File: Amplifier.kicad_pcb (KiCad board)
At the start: 2 copper layers, 63 x 100 mm, 26 parts, among them J1 Input, J2 Conn_01x04, J3 output, T1 Transformer_SP_1S, U1 6N2P, U2 6P14P

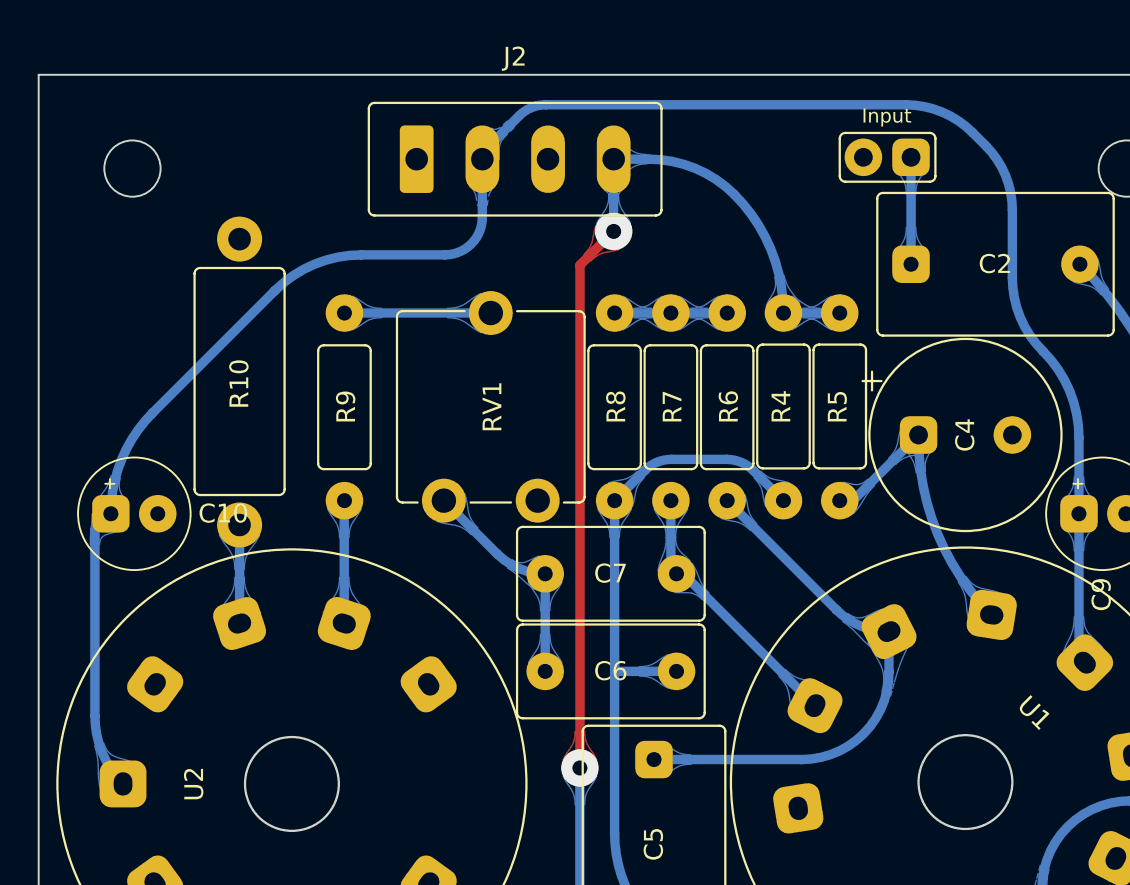
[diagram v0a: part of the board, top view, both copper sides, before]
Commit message: Neon bulb added on the amplifier PCB
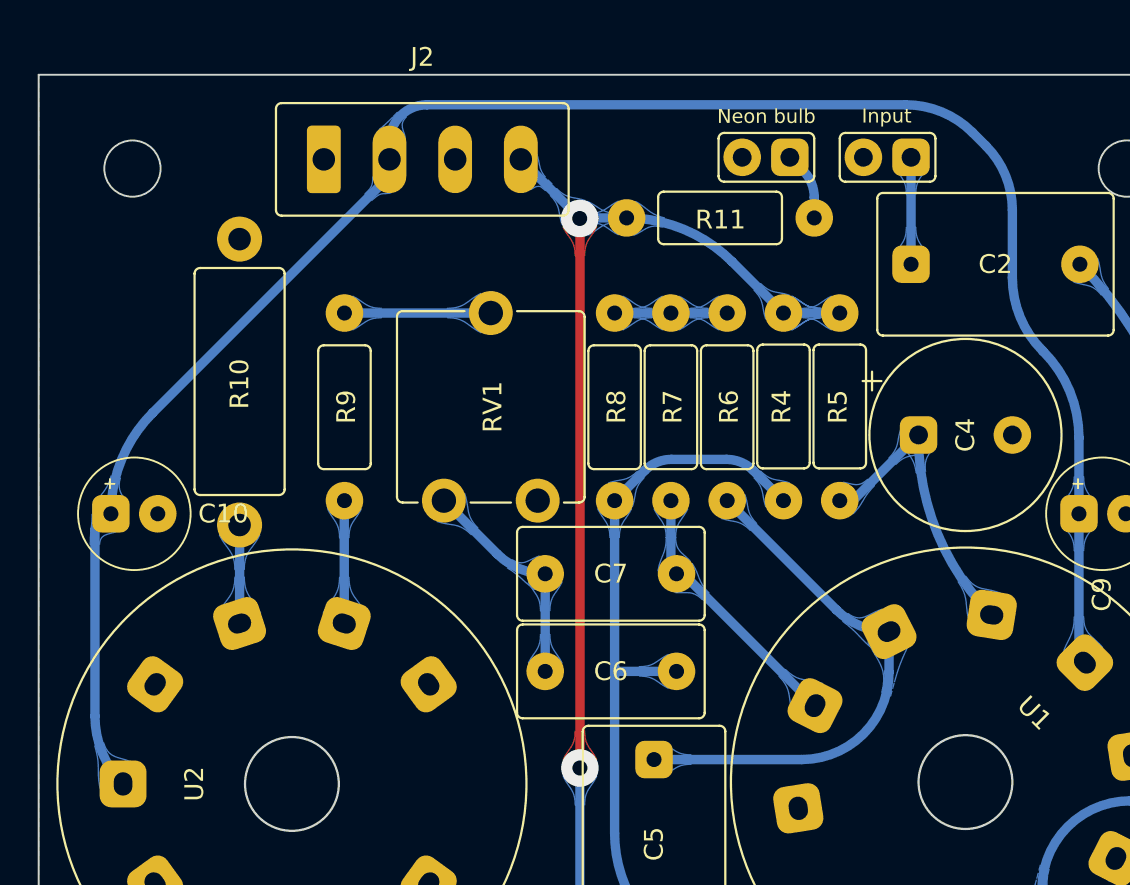
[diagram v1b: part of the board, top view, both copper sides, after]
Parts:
- added J4: Neon bulb, spdf1626_lib:PinHeader_1x02_P2.54mm, F.Cu at (97.0, 44.4)
- added R11: 1M, spdf1626_lib:R_THT_025W, F.Cu at (93.3, 47.6)
- moved J2 4.95 mm to (77.5, 44.5)
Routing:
- net Net-(J4-Pad1): track 0.00 -> 3.67 mm
- net 240V: track 85.8 -> 85.1 mm
- net +6V: track 103.7 -> 103.2 mm

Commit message: Temp
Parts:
- removed T1: Transformer_SP_1S, spdf1626_lib:Output_transformer
- added C1: 10uF, spdf1626_lib:C_THT_D10.0mm_P5.00mm, F.Cu at (64.7, 56.3)
- J2: value Conn_01x04 -> Power
- J3: value output -> Transformer; footprint spdf1626_lib:PinHeader_1x02_P2.54mm -> spdf1626_lib:MCV_1,5_4-G-3.5_1x03_P3.50mm_Vertical
- moved J4 51.6 mm to (101.2, 95.8)
- moved J3 48.9 mm to (76.5, 93.8), turned to 180 degrees
- moved R11 44.9 mm to (100.0, 92.0)
- moved R9 1.10 mm to (74.4, 57.7)
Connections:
- J3 pad 1: Left_output -> 240V
- J3 pad 2: GND -> Net-(U2-Pad9)
- U2 pad 7: Net-(T1-Pad3) -> Net-(U2-Pad7)
- U2 pad 9: Net-(T1-Pad2) -> Net-(U2-Pad9)
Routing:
- net Net-(T1-Pad2): track 30.7 -> 0.00 mm
- net Net-(T1-Pad3): track 19.9 -> 0.00 mm
- net Net-(U2-Pad7): track 0.00 -> 11.2 mm
- net Net-(U2-Pad9): track 0.00 -> 11.2 mm
- net Left_output: track 8.39 -> 0.00 mm
- net 240V: track 85.1 -> 80.4 mm
- net Net-(J4-Pad1): track 3.67 -> 5.35 mm
- net Net-(R9-Pad1): track 7.80 -> 6.70 mm
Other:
- board size 63 x 100 mm -> 68 x 64 mm

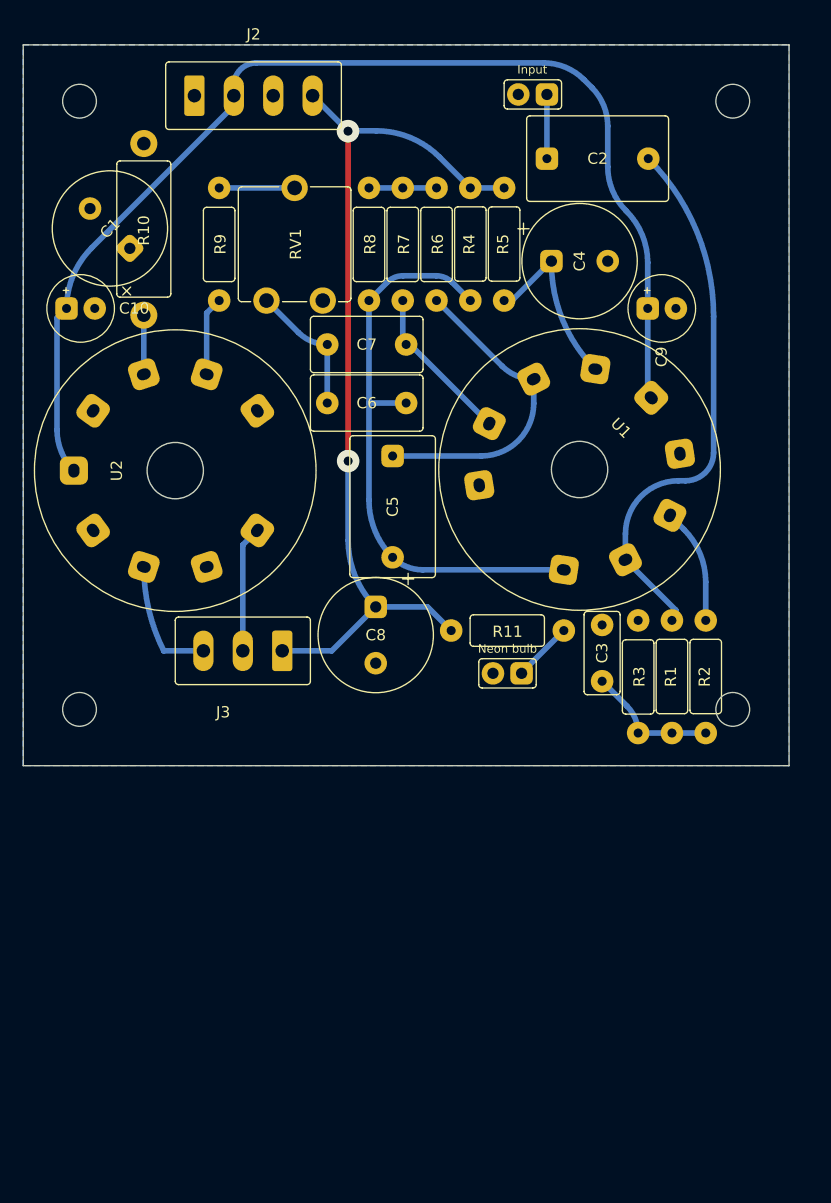
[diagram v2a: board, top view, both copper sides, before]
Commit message: New amplifier PCB with external transformer
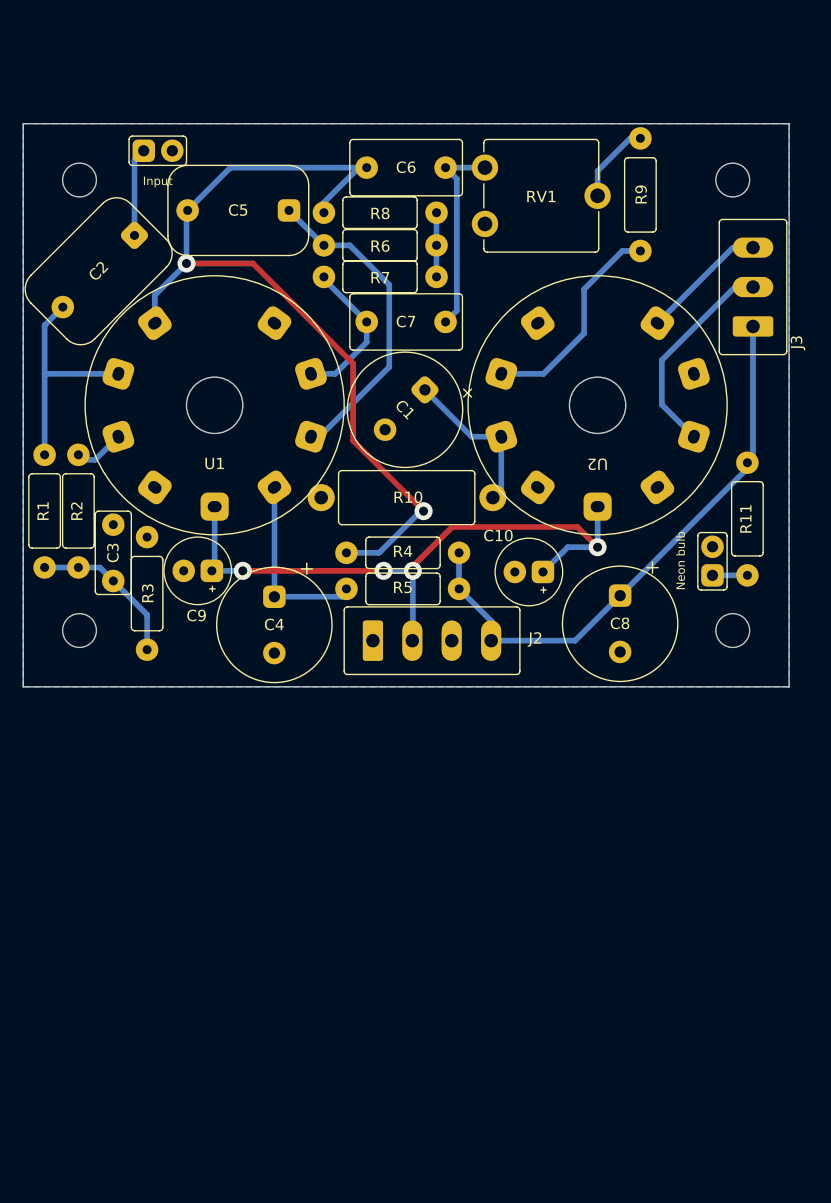
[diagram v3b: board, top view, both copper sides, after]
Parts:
- moved R1 57.6 mm to (58.9, 81.4)
- moved R2 57.6 mm to (61.9, 81.4)
- moved J3 55.6 mm to (121.8, 61.5), turned to 90 degrees
- moved J2 50.9 mm to (93.3, 92.9)
- moved C9 47.3 mm to (72.5, 86.7), turned to 180 degrees
- moved C10 46.2 mm to (101.9, 86.8), turned to 180 degrees
- moved C2 45.4 mm to (63.7, 60.1), turned to -135 degrees
- moved C3 44.3 mm to (65.0, 87.6)
- moved R3 44.2 mm to (68.0, 88.7)
- moved C4 42.2 mm to (79.3, 91.5), turned to -90 degrees
- moved U2 37.9 mm to (108.0, 72.0), turned to 180 degrees
- moved R9 37.7 mm to (111.8, 53.3)
- moved J1 36.1 mm to (67.7, 49.4), turned to 90 degrees
- moved R10 35.0 mm to (98.7, 80.2), turned to 180 degrees
- moved U1 32.9 mm to (74.0, 72.0), turned to 180 degrees
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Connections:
- J3 pad 2: Net-(U2-Pad9) -> Net-(U2-Pad7)
- J3 pad 3: Net-(U2-Pad7) -> Net-(U2-Pad9)
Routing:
- net +6V: track 103.2 -> 58.2 mm, vias 0 -> 4
- net 240V: track 80.4 -> 50.9 mm, vias 2 -> 0
- net Net-(C2-Pad2): track 48.9 -> 20.3 mm
- net Net-(C5-Pad2): track 52.7 -> 77.2 mm, vias 0 -> 2
- net Net-(R9-Pad2): track 7.01 -> 19.2 mm
- net Net-(R10-Pad1): track 5.25 -> 14.3 mm
- net Net-(U2-Pad7): track 11.2 -> 18.8 mm
- net Net-(C6-Pad2): track 12.0 -> 18.0 mm
- net Net-(R2-Pad2): track 10.3 -> 4.58 mm
- net Net-(J4-Pad1): track 5.35 -> 3.10 mm
- net Net-(C3-Pad1): track 11.8 -> 13.9 mm
- net Net-(C2-Pad1): track 5.70 -> 7.86 mm
- net Net-(C7-Pad1): track 14.3 -> 13.5 mm
- net Net-(R9-Pad1): track 6.70 -> 7.20 mm
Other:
- board size 68 x 64 mm -> 68 x 50 mm

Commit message: New Amplifier PCB almost ready
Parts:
- J2: footprint spdf1626_lib:MCV_1,5_4-G-3.5_1x04_P3.50mm_Vertical -> spdf1626_lib:MCV_1,5_4-G-5.0_1x04_P5.0mm_Vertical
- J3: footprint spdf1626_lib:MCV_1,5_4-G-3.5_1x03_P3.50mm_Vertical -> spdf1626_lib:MCV_1,5_4-G-5.0_1x03_P5.0mm_Vertical
- moved C10 12.5 mm to (114.3, 85.2), turned to 0 degrees
- moved R11 12.0 mm to (121.9, 70.1)
- moved R9 10.5 mm to (103.1, 59.2), turned to 180 degrees
- moved C3 8.02 mm to (58.9, 82.4), turned to 0 degrees
- moved R5 7.66 mm to (84.3, 84.1)
- moved R1 7.20 mm to (58.9, 74.2)
- moved R2 7.20 mm to (61.9, 74.2)
- moved J3 7.08 mm to (119.5, 54.8)
- moved C9 5.97 mm to (69.4, 91.8), turned to -90 degrees
- moved R3 5.14 mm to (63.9, 85.6), turned to 180 degrees
- moved J4 4.52 mm to (121.9, 84.5), turned to 0 degrees
- moved R4 3.74 mm to (94.3, 84.1), turned to 180 degrees
- moved J2 1.43 mm to (93.6, 91.5)
- moved C4 1.20 mm to (78.1, 91.4)
- moved C8 0.98 mm to (109.1, 91.8)
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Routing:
- net 240V: track 50.9 -> 63.6 mm
- net Net-(R9-Pad2): track 19.2 -> 10.6 mm
- net Net-(U2-Pad9): track 11.3 -> 19.3 mm
- net Net-(C4-Pad1): track 16.6 -> 10.1 mm
- net Net-(J4-Pad1): track 3.10 -> 9.40 mm
- net Net-(U2-Pad7): track 18.8 -> 24.9 mm
- net Net-(C2-Pad2): track 20.3 -> 14.6 mm
- net Net-(C3-Pad1): track 13.9 -> 9.40 mm
- net +6V: track 58.2 -> 61.8 mm
- net Net-(R2-Pad2): track 4.58 -> 7.06 mm
- net Net-(C5-Pad2): track 77.2 -> 78.4 mm
- net Net-(C7-Pad1): track 13.5 -> 12.3 mm
- net Net-(R9-Pad1): track 7.20 -> 6.50 mm
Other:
- outline, holes or cut-outs redrawn

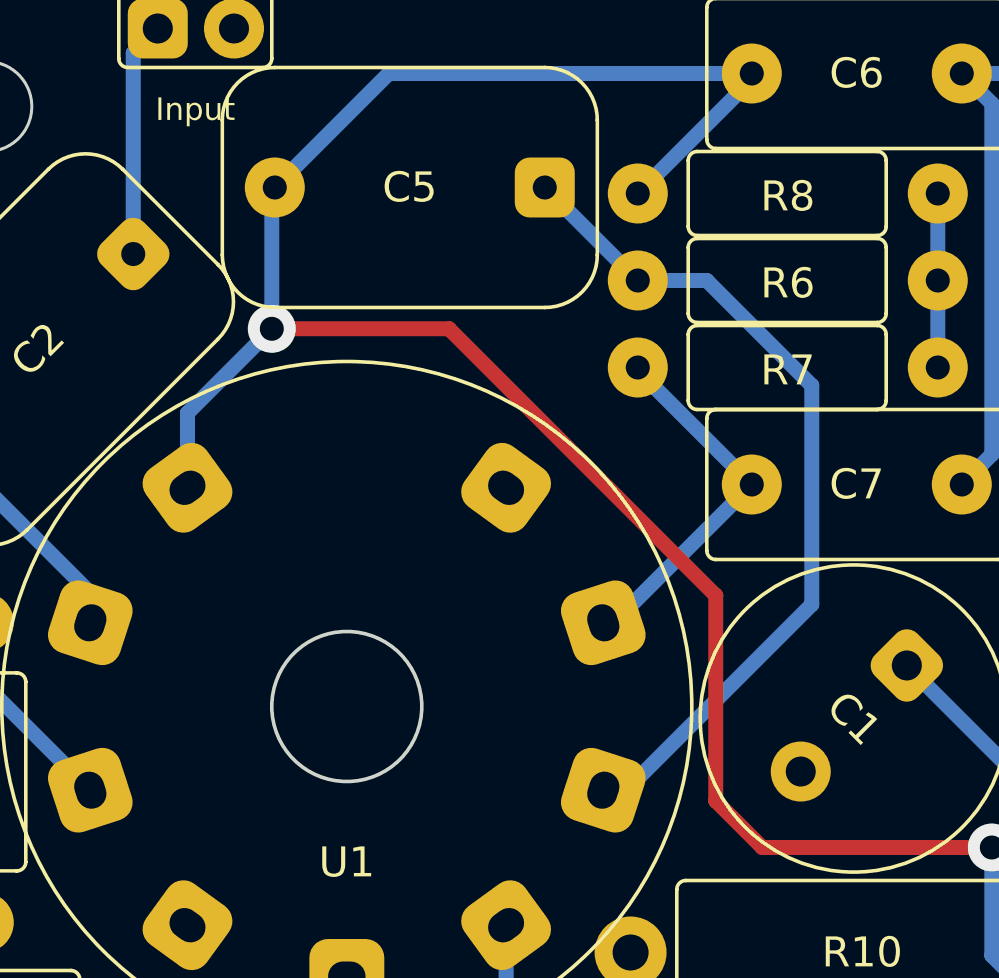
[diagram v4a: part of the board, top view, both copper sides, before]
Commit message: Power supply PCB updated
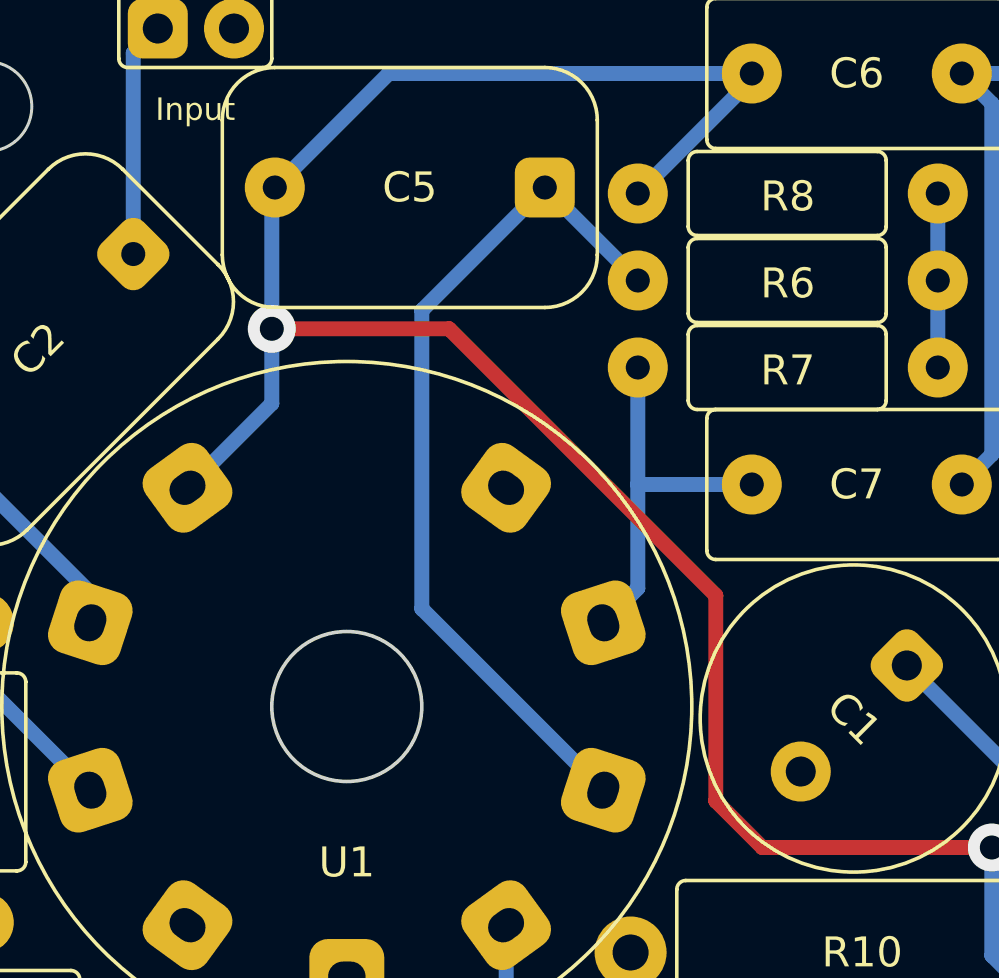
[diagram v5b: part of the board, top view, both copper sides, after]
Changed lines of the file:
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@@
   (segment (start 74 81) (end 74 85.9) (width 0.5) (layer "B.Cu") (net 3))
   (segment (start 108 85.2) (end 108 81) (width 0.5) (layer "B.Cu") (net 3))
-  (segment (start 82.55 69.21) (end 82.89 69.21) (width 0.5) (layer "B.Cu") (net 4))
-  (segment (start 83.7 60.8) (end 87.5 64.6) (width 0.5) (layer "B.Cu") (net 4))
-  (segment (start 82.89 69.21) (end 87.5 64.6) (width 0.5) (layer "B.Cu") (net 4))
-  (segment (start 83.7 60.7) (end 83.7 60.8) (width 0.5) (layer "B.Cu") (net 4))
+  (segment (start 83.7 68.06) (end 82.55 69.21) (width 0.5) (layer "B.Cu") (net 4))
+  (segment (start 87.5 64.6) (end 83.7 64.6) (width 0.5) (layer "B.Cu") (net 4))
+  (segment (start 83.7 64.6) (end 83.7 68.06) (width 0.5) (layer "B.Cu") (net 4))
+  (segment (start 83.7 60.7) (end 83.7 64.6) (width 0.5) (layer "B.Cu") (net 4))
   (segment (start 58.9 85.6) (end 58.9 82.4) (width 0.5) (layer "B.Cu") (net 5))
   (segment (start 58.9 79.2) (end 58.9 82.4) (width 0.5) (layer "B.Cu") (net 5))
@@
   (segment (start 78.1 88.9) (end 79.31 87.69) (width 0.5) (layer "B.Cu") (net 10))
   (segment (start 79.31 87.69) (end 79.31 79.29) (width 0.5) (layer "B.Cu") (net 10))
-  (segment (start 83.7 57.8) (end 86 57.8) (width 0.5) (layer "B.Cu") (net 11))
-  (segment (start 86 57.8) (end 89.5 61.3) (width 0.5) (layer "B.Cu") (net 11))
-  (segment (start 89.5 68.6) (end 83.31 74.79) (width 0.5) (layer "B.Cu") (net 11))
+  (segment (start 82.55 74.79) (end 76.5 68.74) (width 0.5) (layer "B.Cu") (net 11))
   (segment (start 83.7 57.8) (end 80.6 54.7) (width 0.5) (layer "B.Cu") (net 11))
-  (segment (start 89.5 61.3) (end 89.5 68.6) (width 0.5) (layer "B.Cu") (net 11))
-  (segment (start 83.31 74.79) (end 82.55 74.79) (width 0.5) (layer "B.Cu") (net 11))
+  (segment (start 76.5 68.74) (end 76.5 58.8) (width 0.5) (layer "B.Cu") (net 11))
+  (segment (start 76.5 58.8) (end 80.6 54.7) (width 0.5) (layer "B.Cu") (net 11))
   (segment (start 95.5 76.7) (end 87.85 76.7) (width 0.5) (layer "F.Cu") (net 12))
   (segment (start 86.3 68.3) (end 77.41 59.41) (width 0.5) (layer "F.Cu") (net 12))
@@
   (via (at 71.5 59.41) (size 1.6) (drill 0.8) (layers "F.Cu" "B.Cu") (net 12))
   (via (at 95.5 76.7) (size 1.6) (drill 0.8) (layers "F.Cu" "B.Cu") (net 12))
-  (segment (start 68.69 62.22) (end 71.5 59.41) (width 0.5) (layer "B.Cu") (net 12))
   (segment (start 71.5 59.41) (end 71.5 54.8) (width 0.5) (layer "B.Cu") (net 12))
   (segment (start 87.5 51.1) (end 87.5 50.9) (width 0.5) (layer "B.Cu") (net 12))
   (segment (start 95.5 80.3) (end 99.3 84.1) (width 0.5) (layer "B.Cu") (net 12))
-  (segment (start 68.69 64.71) (end 68.69 62.22) (width 0.5) (layer "B.Cu") (net 12))
   (segment (start 83.7 54.9) (end 87.5 51.1) (width 0.5) (layer "B.Cu") (net 12))
+  (segment (start 71.5 59.41) (end 71.5 61.9) (width 0.5) (layer "B.Cu") (net 12))
+  (segment (start 71.5 61.9) (end 68.69 64.71) (width 0.5) (layer "B.Cu") (net 12))
   (segment (start 95.5 76.7) (end 95.5 80.3) (width 0.5) (layer "B.Cu") (net 12))
   (segment (start 75.4 50.9) (end 71.6 54.7) (width 0.5) (layer "B.Cu") (net 12))
